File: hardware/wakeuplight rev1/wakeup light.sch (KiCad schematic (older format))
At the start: 15 parts

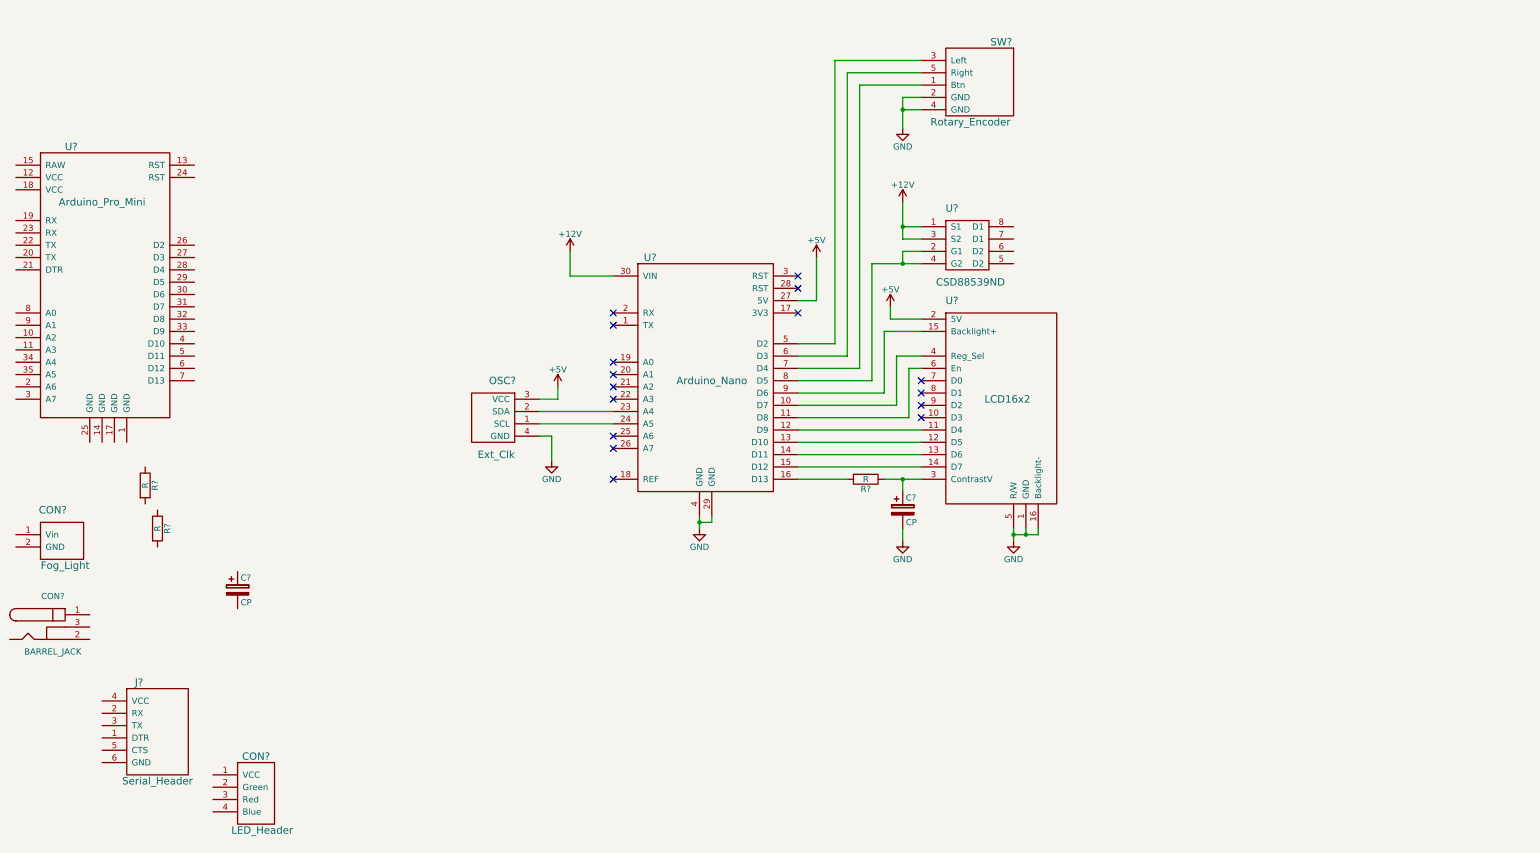
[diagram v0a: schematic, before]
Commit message: updated schematic with a few more wires
connected a few more wires to components, modified the serial header to
fit nicer in schematic
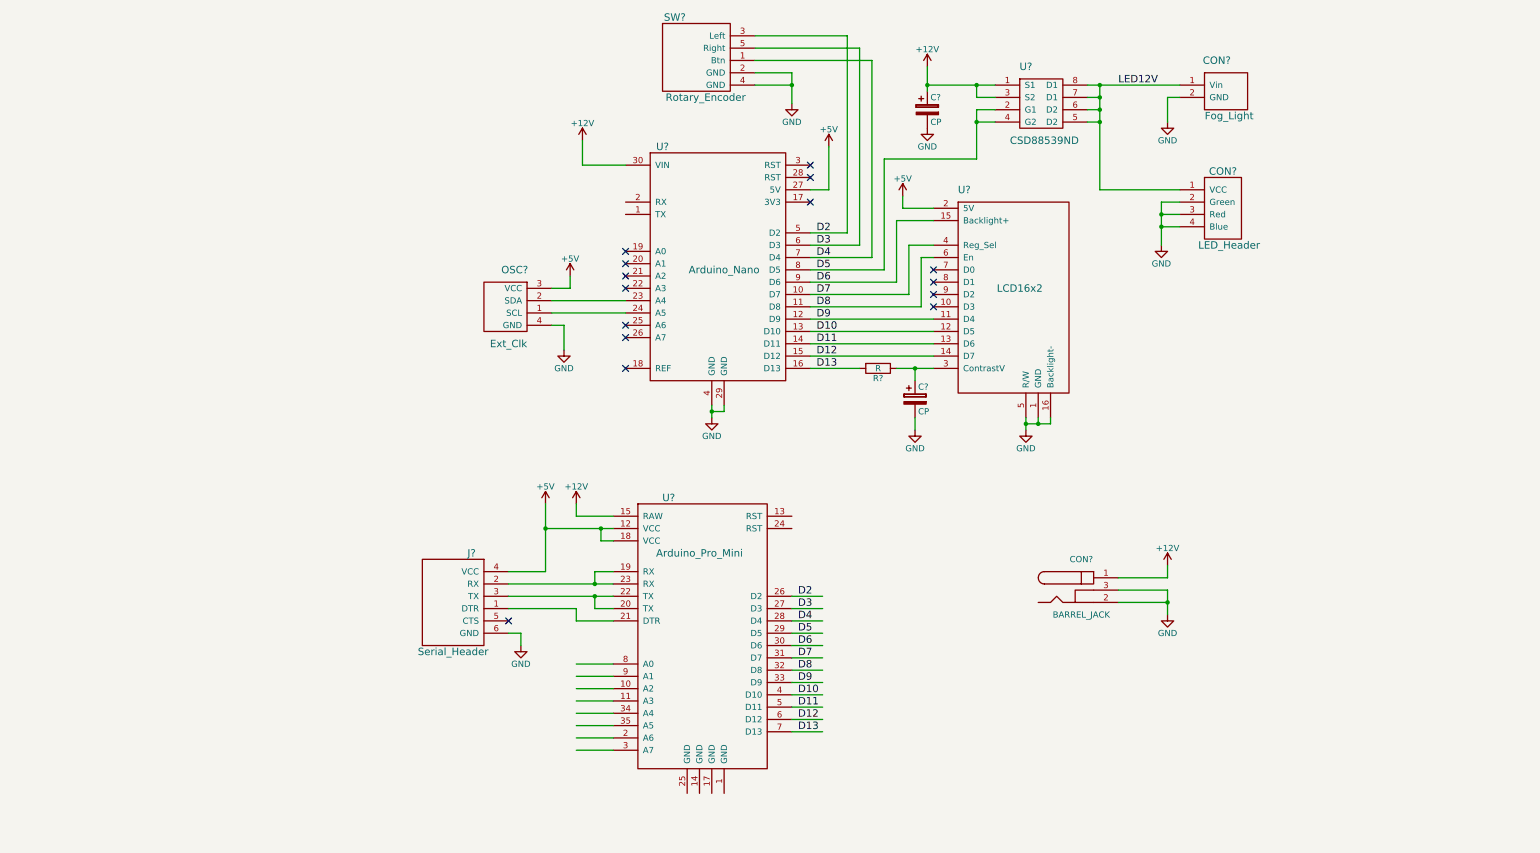
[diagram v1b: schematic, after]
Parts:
- removed J?: Serial_Header, symbol Serial_Header
- removed R? (x2): R, symbol R
- added J?: Serial_Header, symbol Serial_Header
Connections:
- net labels added: D10, D11, D12, D13, D2, D3, D4, D5, D6, D7, D8, D9, LED12V
- wire segments 56 -> 113
- no-connect marks 16 -> 15
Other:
- moved on the sheet: C?, CON?, OSC?, R?, SW?, U?

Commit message: Completed rough schematic
Everything should be there.
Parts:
- added R? (x2): R, symbol R
- added U?: CSD88539ND, symbol CSD88539ND
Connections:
- net labels added: A0, A1, SCL, SDA, SDL
- net labels removed: LED12V
- wire segments 113 -> 122
- no-connect marks 15 -> 19
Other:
- moved on the sheet: C?, CON?, SW?, U?

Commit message: DRC on schematic is complete
Modified pins on symbols to appropriate electrical type (input, output,
bidirectional, etc)
Annotated schematics
Resolved all DRC errors.
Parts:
- removed CON?: LED_Header, symbol LED_Header
- removed U?: Arduino_Nano, symbol Arduino_Nano
- removed U?: Arduino_Pro_Mini, symbol Arduino_Pro_Mini
- removed U?: LCD16x2, symbol LCD16x2
- added CON3: LED_Header, symbol LED_Header
- added U1: Arduino_Pro_Mini, symbol Arduino_Pro_Mini
- added U2: Arduino_Nano, symbol Arduino_Nano
- added U3: LCD16x2, symbol LCD16x2
- gave numbers to parts that had none: 12
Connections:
- net labels removed: SDL
- wire segments 122 -> 130
- no-connect marks 19 -> 21
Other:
- note added: "VCC is the same as\n5V on Pro Mini"

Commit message: updated netlist and linked components to footprints
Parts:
- C1, C2: footprint (none) -> wakeuplight rev1:Cap_Fat_1000uF_25V
- CON1: footprint (none) -> Connect:BARREL_JACK
- CON2: footprint (none) -> wakeuplight rev1:Fog_Light
- CON3: footprint (none) -> Pin_Headers:Pin_Header_Straight_1x04
- J1: footprint (none) -> Pin_Headers:Pin_Header_Straight_1x06
- OSC1: footprint (none) -> wakeuplight rev1:External_Clock
- R1, R2, R3: footprint (none) -> Resistors_SMD:R_0603_HandSoldering
- SW1: footprint (none) -> wakeuplight rev1:Push_Button
- U1: footprint (none) -> wakeuplight rev1:Arduino_Pro_Mini
- U2: footprint (none) -> wakeuplight rev1:Arduino_Nano
- U3: footprint (none) -> wakeuplight rev1:LCD_16x2
- U4, U5: footprint (none) -> SMD_Packages:SOIC-8-N
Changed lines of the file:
@@
 F 0 "CON2" H 8450 4300 60  0000 C CNN
 F 1 "Fog_Light" H 8550 3850 60  0000 C CNN
-F 2 "" H 8100 4000 60  0000 C CNN
+F 2 "wakeuplight rev1:Fog_Light" H 8100 4000 60  0001 C CNN
 F 3 "" H 8100 4000 60  0000 C CNN
 	1    8250 4100
@@
 F 0 "CON1" H 6500 5750 50  0000 C CNN
 F 1 "BARREL_JACK" H 6500 5300 50  0000 C CNN
-F 2 "" H 6500 5500 50  0000 C CNN
+F 2 "Connect:BARREL_JACK" H 6500 5500 50  0001 C CNN
 F 3 "" H 6500 5500 50  0000 C CNN
 	1    6500 5500
@@
 F 0 "R3" V 4930 3700 50  0000 C CNN
 F 1 "R" V 4850 3700 50  0000 C CNN
-F 2 "" V 4780 3700 50  0000 C CNN
+F 2 "Resistors_SMD:R_0603_HandSoldering" V 4780 3700 50  0001 C CNN
 F 3 "" H 4850 3700 50  0000 C CNN
 	1    4850 3700
@@
 F 0 "C1" H 5175 4050 50  0000 L CNN
 F 1 "CP" H 5175 3850 50  0000 L CNN
-F 2 "" H 5188 3800 50  0000 C CNN
+F 2 "wakeuplight rev1:Cap_Fat_1000uF_25V" H 5188 3800 50  0001 C CNN
 F 3 "" H 5150 3950 50  0000 C CNN
 	1    5150 3950
@@
 F 0 "C2" H 9025 2150 50  0000 L CNN
 F 1 "CP" H 9025 1950 50  0000 L CNN
-F 2 "" H 9038 1900 50  0000 C CNN
+F 2 "wakeuplight rev1:Cap_Fat_1000uF_25V" H 9038 1900 50  0001 C CNN
 F 3 "" H 9000 2050 50  0000 C CNN
 	1    9000 2050
@@
 F 0 "OSC1" H 2400 3700 60  0000 C CNN
 F 1 "Ext_Clk" H 2450 3100 60  0000 C CNN
-F 2 "" H 2150 3300 60  0000 C CNN
+F 2 "wakeuplight rev1:External_Clock" H 2150 3300 60  0001 C CNN
 F 3 "" H 2150 3300 60  0000 C CNN
 	1    2150 3300
@@
 F 0 "U5" H 9350 3700 60  0000 C CNN
 F 1 "CSD88539ND" H 9500 3100 60  0000 C CNN
-F 2 "" H 9450 3300 60  0000 C CNN
+F 2 "SMD_Packages:SOIC-8-N" H 9450 3300 60  0001 C CNN
 F 3 "" H 9450 3300 60  0000 C CNN
 	1    9450 3300
@@
 F 0 "SW1" H 1100 2150 60  0000 C CNN
 F 1 "Rotary_Encoder" H 1350 1500 60  0000 C CNN
-F 2 "" H 950 1950 60  0000 C CNN
+F 2 "wakeuplight rev1:Push_Button" H 950 1950 60  0001 C CNN
 F 3 "" H 950 1950 60  0000 C CNN
 	1    950  1950
@@
 F 0 "J1" H 1350 5900 60  0000 C CNN
 F 1 "Serial_Header" H 1500 5100 60  0000 C CNN
-F 2 "" H 950 5550 60  0000 C CNN
+F 2 "Pin_Headers:Pin_Header_Straight_1x06" H 950 5550 60  0001 C CNN
 F 3 "" H 950 5550 60  0000 C CNN
 	1    1450 5550
@@
 F 0 "R1" V 2480 1650 50  0000 C CNN
 F 1 "R" V 2400 1650 50  0000 C CNN
-F 2 "" V 2330 1650 50  0000 C CNN
+F 2 "Resistors_SMD:R_0603_HandSoldering" V 2330 1650 50  0001 C CNN
 F 3 "" H 2400 1650 50  0000 C CNN
 	1    2400 1650
@@
 F 0 "R2" V 2630 1650 50  0000 C CNN
 F 1 "R" V 2550 1650 50  0000 C CNN
-F 2 "" V 2480 1650 50  0000 C CNN
+F 2 "Resistors_SMD:R_0603_HandSoldering" V 2480 1650 50  0001 C CNN
 F 3 "" H 2550 1650 50  0000 C CNN
 	1    2550 1650
@@
 F 0 "U4" H 9250 4750 60  0000 C CNN
 F 1 "CSD88539ND" H 9400 4150 60  0000 C CNN
-F 2 "" H 9350 4350 60  0000 C CNN
+F 2 "SMD_Packages:SOIC-8-N" H 9350 4350 60  0001 C CNN
 F 3 "" H 9350 4350 60  0000 C CNN
 	1    9350 4350
@@
 F 0 "U3" H 5550 3750 60  0000 C CNN
 F 1 "LCD16x2" H 6000 2950 60  0000 C CNN
-F 2 "" H 6100 3000 60  0000 C CNN
+F 2 "wakeuplight rev1:LCD_16x2" H 6100 3000 60  0001 C CNN
 F 3 "" H 6100 3000 60  0000 C CNN
 	1    5900 3000
@@
 F 0 "U2" H 3100 3700 60  0000 C CNN
 F 1 "Arduino_Nano" H 3600 2700 60  0000 C CNN
-F 2 "" H 3300 2500 60  0000 C CNN
+F 2 "wakeuplight rev1:Arduino_Nano" H 3300 2500 60  0001 C CNN
 F 3 "" H 3300 2500 60  0000 C CNN
 	1    3600 2800
@@
 F 0 "U1" H 3150 6650 60  0000 C CNN
 F 1 "Arduino_Pro_Mini" H 3400 6200 60  0000 C CNN
-F 2 "" H 3050 5950 60  0000 C CNN
+F 2 "wakeuplight rev1:Arduino_Pro_Mini" H 3050 5950 60  0001 C CNN
 F 3 "" H 3050 5950 60  0000 C CNN
 	1    3050 5700
@@
 F 0 "CON3" H 9050 2900 60  0000 C CNN
 F 1 "LED_Header" H 9100 2300 60  0000 C CNN
-F 2 "" H 8500 2550 60  0000 C CNN
+F 2 "Pin_Headers:Pin_Header_Straight_1x04" H 8500 2550 60  0001 C CNN
 F 3 "" H 8500 2550 60  0000 C CNN
 	1    8500 2550
